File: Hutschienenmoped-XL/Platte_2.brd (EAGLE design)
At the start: 107 x 45 mm, 0 parts

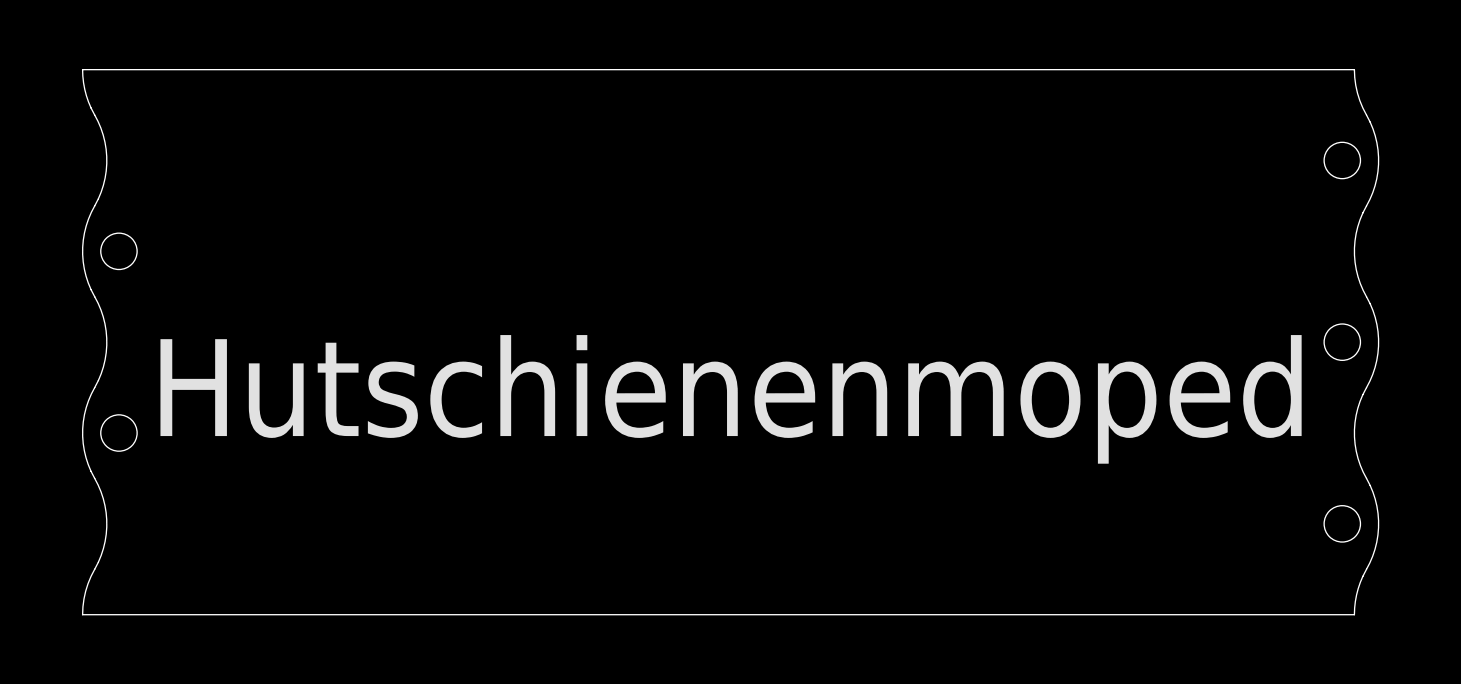
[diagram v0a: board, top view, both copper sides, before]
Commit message: Update wire coordinates and add new wires and circles.
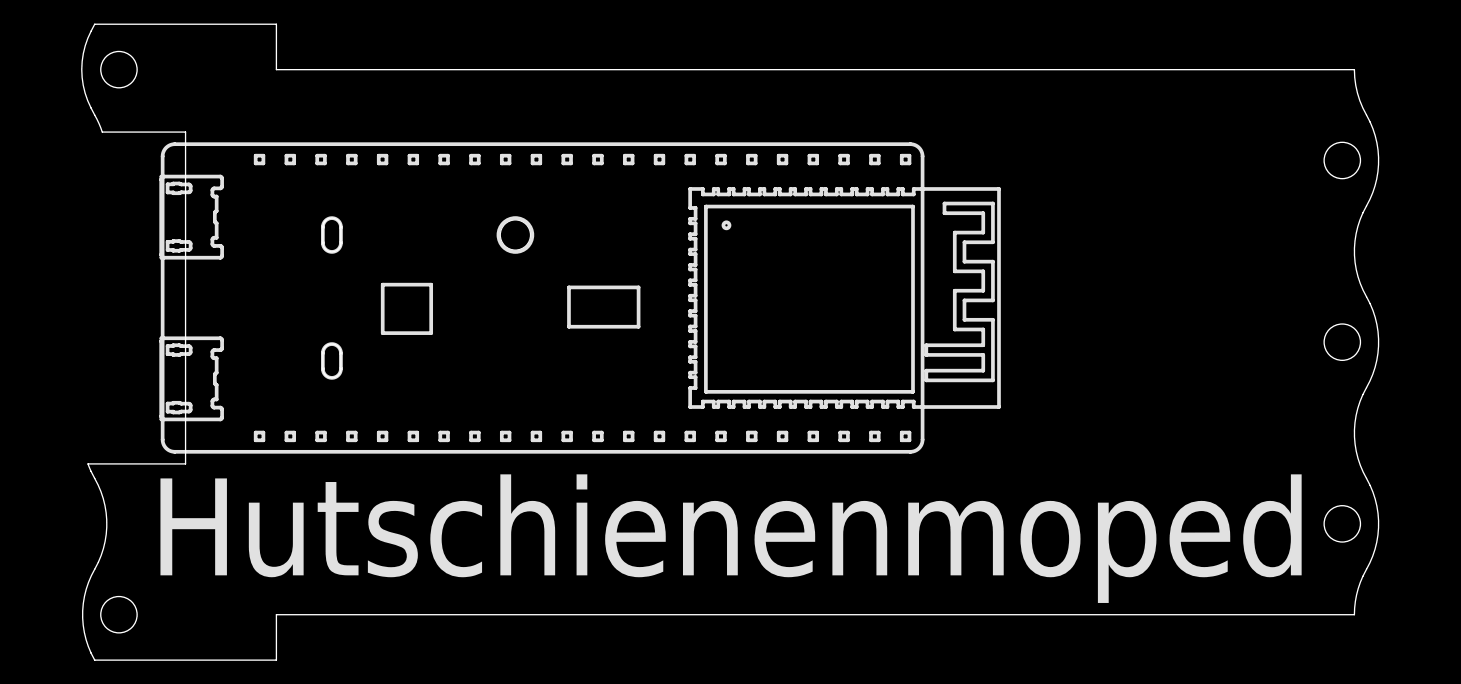
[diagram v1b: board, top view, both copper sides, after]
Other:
- board size 107 x 45 mm -> 107.1 x 52.5 mm
